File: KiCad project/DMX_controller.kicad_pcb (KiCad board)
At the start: 2 copper layers, 139.7 x 121.9 mm, 12 parts, among them J1 DMX_output, SW1 SW_Push_DPDT, U1 TTL_to_RS485_transceiver

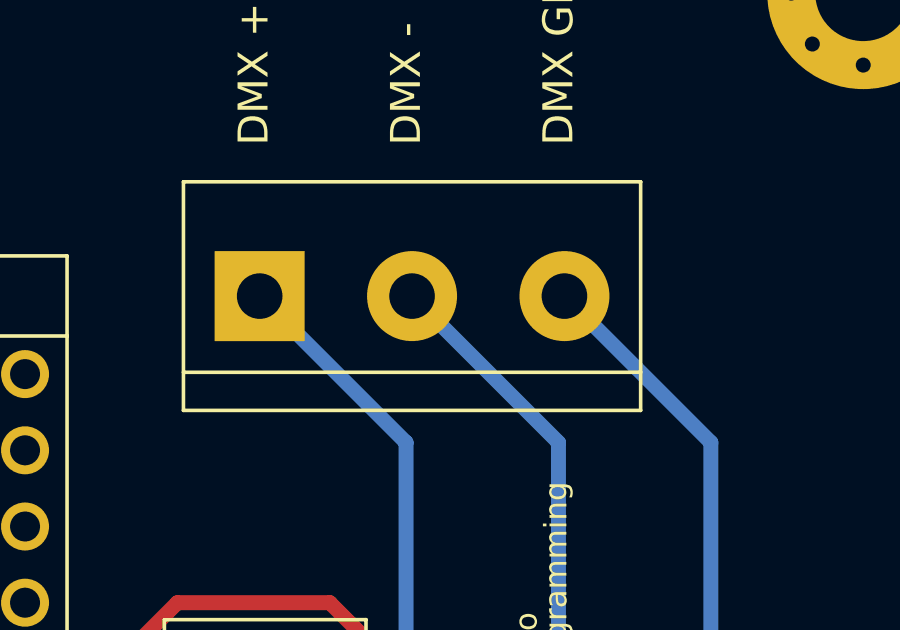
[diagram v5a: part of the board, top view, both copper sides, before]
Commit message: Rotate screw terminal so 3D model is oriented
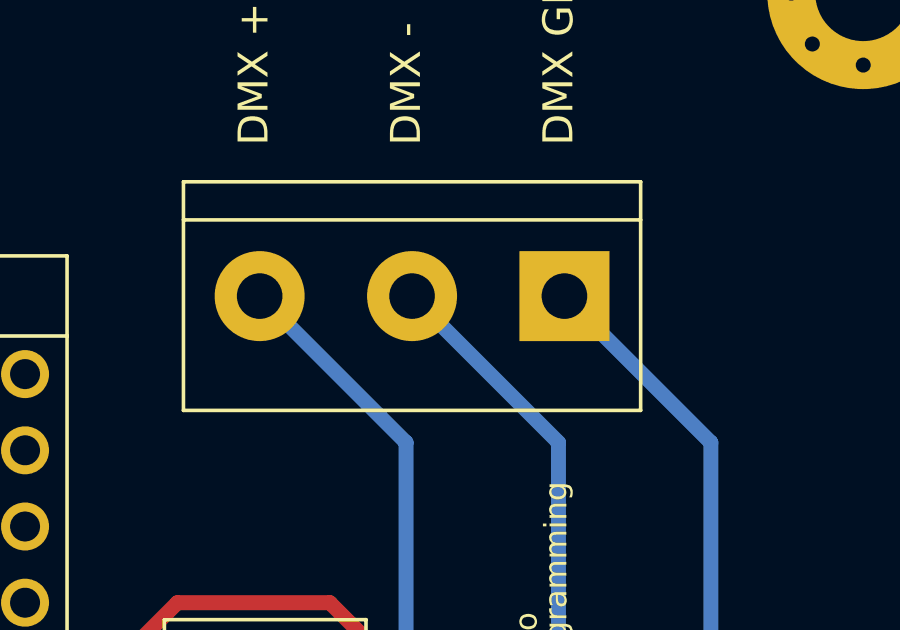
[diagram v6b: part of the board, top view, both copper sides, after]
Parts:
- moved J1 10.2 mm to (167.8, 53.3), turned to 180 degrees
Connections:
- U1 pad 5: Net-(J1-Pad1) -> Net-(J1-Pad3)
- U1 pad 7: Net-(J1-Pad3) -> Net-(J1-Pad1)
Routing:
- net Net-(J1-Pad3): track 118.7 -> 95.7 mm
- net Net-(J1-Pad1): track 95.7 -> 118.7 mm
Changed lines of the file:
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@@
       (net 4 "GND") (pinfunction "GND") (pintype "power_in"))
     (pad "5" thru_hole circle (at 41.5 3 180) (size 2 2) (drill 1) (layers *.Cu *.Mask)
-      (net 30 "Net-(J1-Pad1)") (pinfunction "A+") (pintype "output"))
+      (net 32 "Net-(J1-Pad3)") (pinfunction "A+") (pintype "output"))
     (pad "6" thru_hole circle (at 41.5 7.75 180) (size 2 2) (drill 1) (layers *.Cu *.Mask)
       (net 31 "Net-(J1-Pad2)") (pinfunction "B-") (pintype "output"))
     (pad "7" thru_hole circle (at 41.5 12.5 180) (size 2 2) (drill 1) (layers *.Cu *.Mask)
-      (net 32 "Net-(J1-Pad3)") (pinfunction "GND") (pintype "power_in"))
+      (net 30 "Net-(J1-Pad1)") (pinfunction "GND") (pintype "power_in"))
   )
   (footprint "MountingHole:MountingHole_3.2mm_M3_Pad_Via" (layer "F.Cu")
@@
   )
   (footprint "TerminalBlock:TerminalBlock_bornier-3_P5.08mm" (layer "F.Cu")
-    (at 157.68 53.28)
+    (at 167.84 53.28 180)
     (descr "simple 3-pin terminal block, pitch 5.08mm, revamped version of bornier3")
     (tags "terminal block bornier3")
@@
     (fp_line (start 12.63 -3.75) (end 12.63 3.75) (layer "F.Fab") (width 0.1))
     (fp_line (start -2.47 2.55) (end 12.63 2.55) (layer "F.Fab") (width 0.1))
-    (pad "1" thru_hole rect (at 0 0) (size 3 3) (drill 1.52) (layers *.Cu *.Mask)
+    (pad "1" thru_hole rect (at 0 0 180) (size 3 3) (drill 1.52) (layers *.Cu *.Mask)
       (net 30 "Net-(J1-Pad1)") (pinfunction "Pin_1") (pintype "passive"))
-    (pad "2" thru_hole circle (at 5.08 0) (size 3 3) (drill 1.52) (layers *.Cu *.Mask)
+    (pad "2" thru_hole circle (at 5.08 0 180) (size 3 3) (drill 1.52) (layers *.Cu *.Mask)
       (net 31 "Net-(J1-Pad2)") (pinfunction "Pin_2") (pintype "passive"))
-    (pad "3" thru_hole circle (at 10.16 0) (size 3 3) (drill 1.52) (layers *.Cu *.Mask)
+    (pad "3" thru_hole circle (at 10.16 0 180) (size 3 3) (drill 1.52) (layers *.Cu *.Mask)
       (net 32 "Net-(J1-Pad3)") (pinfunction "Pin_3") (pintype "passive"))
     (model "${KICAD6_3DMODEL_DIR}/TerminalBlock.3dshapes/TerminalBlock_bornier-3_P5.08mm.wrl"
@@
   (segment (start 134.62 83.82) (end 145.895255 95.095255) (width 0.5) (layer "B.Cu") (net 27))
   (segment (start 101.655 61.825) (end 84.115 61.825) (width 0.5) (layer "B.Cu") (net 27))
-  (segment (start 162.56 58.16) (end 157.68 53.28) (width 0.5) (layer "B.Cu") (net 30))
-  (segment (start 162.56 124.777204) (end 162.56 58.16) (width 0.5) (layer "B.Cu") (net 30))
-  (segment (start 146.895255 140.441949) (end 162.56 124.777204) (width 0.5) (layer "B.Cu") (net 30))
+  (segment (start 172.72 58.16) (end 172.72 124.46) (width 0.5) (layer "B.Cu") (net 30))
+  (segment (start 152.4 144.78) (end 172.72 124.46) (width 0.5) (layer "B.Cu") (net 30))
+  (segment (start 141.733306 144.78) (end 137.395255 140.441949) (width 0.5) (layer "B.Cu") (net 30))
+  (segment (start 152.4 144.78) (end 141.733306 144.78) (width 0.5) (layer "B.Cu") (net 30))
+  (segment (start 172.72 58.16) (end 167.84 53.28) (width 0.5) (layer "B.Cu") (net 30))
   (segment (start 167.64 58.16) (end 167.64 124.46) (width 0.5) (layer "B.Cu") (net 31))
   (segment (start 143.943306 142.24) (end 142.145255 140.441949) (width 0.5) (layer "B.Cu") (net 31))
+  (segment (start 167.64 58.16) (end 162.76 53.28) (width 0.5) (layer "B.Cu") (net 31))
   (segment (start 149.86 142.24) (end 143.943306 142.24) (width 0.5) (layer "B.Cu") (net 31))
   (segment (start 149.86 142.24) (end 167.64 124.46) (width 0.5) (layer "B.Cu") (net 31))
-  (segment (start 162.76 53.28) (end 167.64 58.16) (width 0.5) (layer "B.Cu") (net 31))
-  (segment (start 172.72 58.16) (end 172.72 124.46) (width 0.5) (layer "B.Cu") (net 32))
-  (segment (start 152.4 144.78) (end 172.72 124.46) (width 0.5) (layer "B.Cu") (net 32))
-  (segment (start 141.733306 144.78) (end 137.395255 140.441949) (width 0.5) (layer "B.Cu") (net 32))
-  (segment (start 152.4 144.78) (end 141.733306 144.78) (width 0.5) (layer "B.Cu") (net 32))
-  (segment (start 167.84 53.28) (end 172.72 58.16) (width 0.5) (layer "B.Cu") (net 32))
+  (segment (start 162.56 124.777204) (end 162.56 58.16) (width 0.5) (layer "B.Cu") (net 32))
+  (segment (start 162.56 58.16) (end 157.68 53.28) (width 0.5) (layer "B.Cu") (net 32))
+  (segment (start 146.895255 140.441949) (end 162.56 124.777204) (width 0.5) (layer "B.Cu") (net 32))
   (segment (start 143.395255 100.441949) (end 156.5325 87.304704) (width 0.5) (layer "F.Cu") (net 33))
   (segment (start 156.5325 87.304704) (end 156.5325 72.1225) (width 0.5) (layer "F.Cu") (net 33))
